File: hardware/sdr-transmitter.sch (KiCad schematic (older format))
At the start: 0 parts

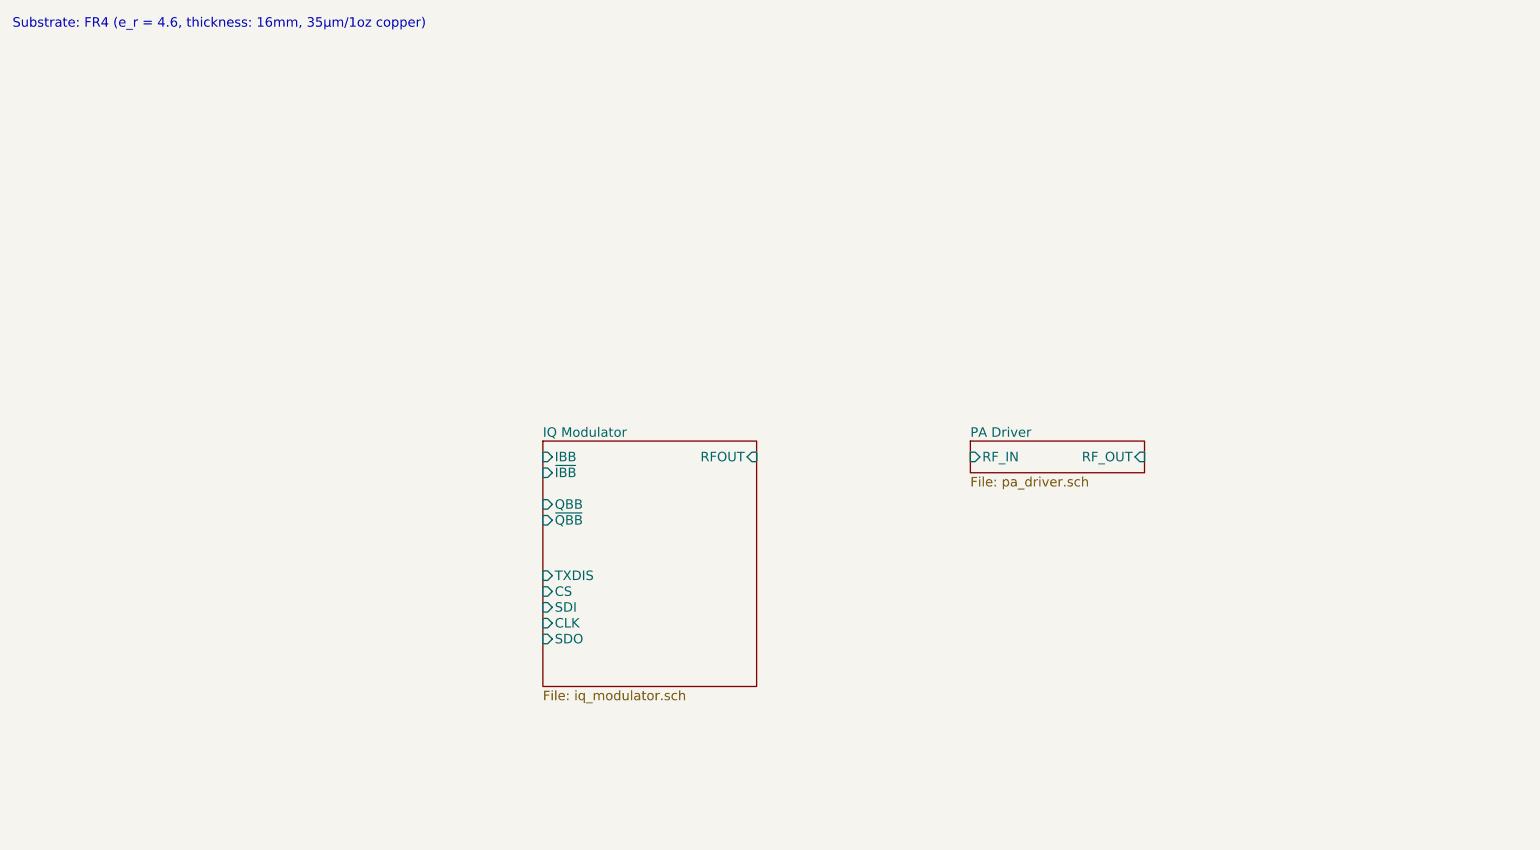
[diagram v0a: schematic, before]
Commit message: Add PA schematic
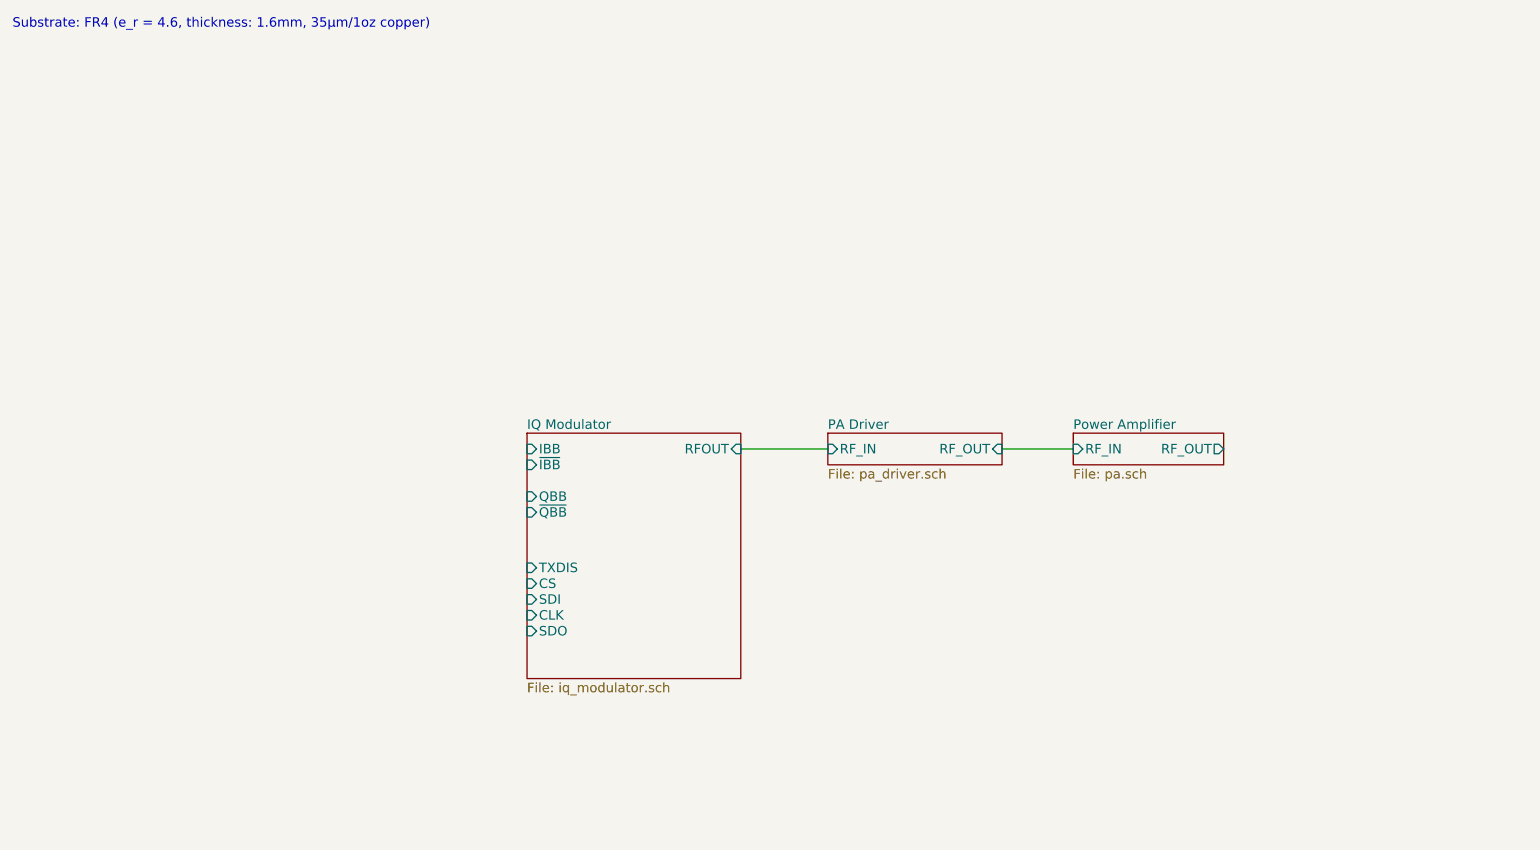
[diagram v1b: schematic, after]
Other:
- note added: "Substrate: FR4 (e_r = 4.6, thickness: 1.6mm, 35µm/1oz copper)"
- note removed: "Substrate: FR4 (e_r = 4.6, thickness: 16mm, 35µm/1oz copper)"
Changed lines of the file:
@@
 LIBS:valves
 LIBS:sdr-transmitter
-LIBS:sdr-transmitter-old
 LIBS:sdr-transmitter-cache
 EELAYER 25 0
@@
 $Descr A4 11693 8268
 encoding utf-8
-Sheet 1 3
+Sheet 1 4
 Title ""
 Date ""
@@
 $EndDescr
 $Sheet
-S 6650 3250 1100 200
+S 5750 3200 1100 200
 U 5A1F13A2
 F0 "PA Driver" 60
 F1 "pa_driver.sch" 60
-F2 "RF_IN" I L 6650 3350 60
-F3 "RF_OUT" I R 7750 3350 60
+F2 "RF_IN" I L 5750 3300 60
+F3 "RF_OUT" I R 6850 3300 60
 $EndSheet
 Text Notes 600  650  0    60   ~ 0
-Substrate: FR4 (e_r = 4.6, thickness: 16mm, 35µm/1oz copper)
+Substrate: FR4 (e_r = 4.6, thickness: 1.6mm, 35µm/1oz copper)
 $Sheet
-S 3950 3250 1350 1550
+S 3850 3200 1350 1550
 U 5A22ED7D
 F0 "IQ Modulator" 60
 F1 "iq_modulator.sch" 60
-F2 "RFOUT" I R 5300 3350 60
-F3 "IBB" I L 3950 3350 60
-F4 "~IBB" I L 3950 3450 60
-F5 "QBB" I L 3950 3650 60
-F6 "TXDIS" I L 3950 4100 60
-F7 "CS" I L 3950 4200 60
-F8 "SDI" I L 3950 4300 60
-F9 "CLK" I L 3950 4400 60
-F10 "SDO" I L 3950 4500 60
-F11 "~QBB" I L 3950 3750 60
+F2 "RFOUT" I R 5200 3300 60
+F3 "IBB" I L 3850 3300 60
+F4 "~IBB" I L 3850 3400 60
+F5 "QBB" I L 3850 3600 60
+F6 "TXDIS" I L 3850 4050 60
+F7 "CS" I L 3850 4150 60
+F8 "SDI" I L 3850 4250 60
+F9 "CLK" I L 3850 4350 60
+F10 "SDO" I L 3850 4450 60
+F11 "~QBB" I L 3850 3700 60
 $EndSheet
+$Sheet
+S 7300 3200 950  200
+U 5A2AAB8B
+F0 "Power Amplifier" 60
+F1 "pa.sch" 60
+F2 "RF_IN" I L 7300 3300 60
+F3 "RF_OUT" O R 8250 3300 60
+$EndSheet
+Wire Wire Line
+	5200 3300 5750 3300
+Wire Wire Line
+	6850 3300 7300 3300
 $EndSCHEMATC

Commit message: Update PA matching circuits
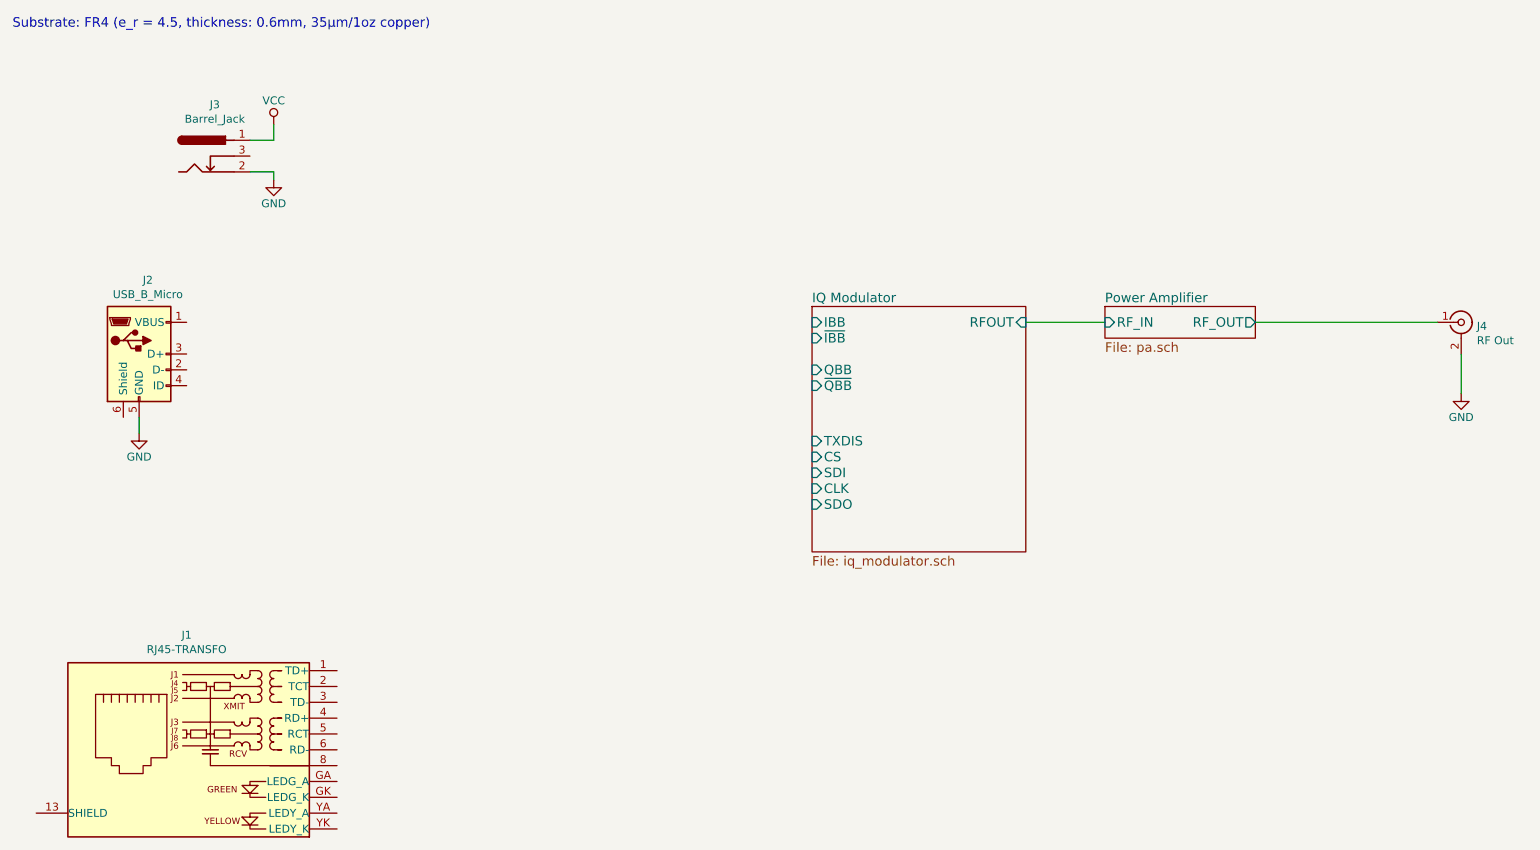
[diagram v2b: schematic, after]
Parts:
- added J1: RJ45-TRANSFO, symbol Connector:RJ45-TRANSFO
- added J2: USB_B_Micro, symbol Connector:USB_B_Micro
- added J3: Barrel_Jack, Connectors:Barrel_Jack_CUI_PJ-036AH-SMT, symbol Connector:Barrel_Jack
- added J4: RF Out, symbol Connector:Conn_Coaxial
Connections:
- net Power Amplifier/RF_OUT: now also J4.1 (In)
- new net GND: J2.5 (GND), J3.2, J4.2 (Ext)
- new net VCC: J3.1
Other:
- note added: "Substrate: FR4 (e_r = 4.5, thickness: 0.6mm, 35µm/1oz copper)"
- note removed: "Substrate: FR4 (e_r = 4.6, thickness: 1.6mm, 35µm/1oz copper)"
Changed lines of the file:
@@
-EESchema Schematic File Version 2
-LIBS:power
-LIBS:device
-LIBS:switches
-LIBS:relays
-LIBS:motors
-LIBS:transistors
-LIBS:conn
-LIBS:linear
-LIBS:regul
-LIBS:74xx
-LIBS:cmos4000
-LIBS:adc-dac
-LIBS:memory
-LIBS:xilinx
-LIBS:microcontrollers
-LIBS:dsp
-LIBS:microchip
-LIBS:analog_switches
-LIBS:motorola
-LIBS:texas
-LIBS:intel
-LIBS:audio
-LIBS:interface
-LIBS:digital-audio
-LIBS:philips
-LIBS:display
-LIBS:cypress
-LIBS:siliconi
-LIBS:opto
-LIBS:atmel
-LIBS:contrib
-LIBS:valves
-LIBS:sdr-transmitter
+EESchema Schematic File Version 4
 LIBS:sdr-transmitter-cache
-EELAYER 25 0
+EELAYER 26 0
 EELAYER END
 $Descr A4 11693 8268
 encoding utf-8
-Sheet 1 4
+Sheet 1 3
 Title ""
 Date ""
@@
 Comment4 ""
 $EndDescr
+Text Notes 600  650  0    60   ~ 0
+Substrate: FR4 (e_r = 4.5, thickness: 0.6mm, 35µm/1oz copper)
 $Sheet
-S 5750 3200 1100 200
-U 5A1F13A2
-F0 "PA Driver" 60
-F1 "pa_driver.sch" 60
-F2 "RF_IN" I L 5750 3300 60
-F3 "RF_OUT" I R 6850 3300 60
-$EndSheet
-Text Notes 600  650  0    60   ~ 0
-Substrate: FR4 (e_r = 4.6, thickness: 1.6mm, 35µm/1oz copper)
-$Sheet
-S 3850 3200 1350 1550
+S 5650 2400 1350 1550
 U 5A22ED7D
 F0 "IQ Modulator" 60
 F1 "iq_modulator.sch" 60
-F2 "RFOUT" I R 5200 3300 60
-F3 "IBB" I L 3850 3300 60
-F4 "~IBB" I L 3850 3400 60
-F5 "QBB" I L 3850 3600 60
-F6 "TXDIS" I L 3850 4050 60
-F7 "CS" I L 3850 4150 60
-F8 "SDI" I L 3850 4250 60
-F9 "CLK" I L 3850 4350 60
-F10 "SDO" I L 3850 4450 60
-F11 "~QBB" I L 3850 3700 60
+F2 "RFOUT" I R 7000 2500 60
+F3 "IBB" I L 5650 2500 60
+F4 "~IBB" I L 5650 2600 60
+F5 "QBB" I L 5650 2800 60
+F6 "TXDIS" I L 5650 3250 60
+F7 "CS" I L 5650 3350 60
+F8 "SDI" I L 5650 3450 60
+F9 "CLK" I L 5650 3550 60
+F10 "SDO" I L 5650 3650 60
+F11 "~QBB" I L 5650 2900 60
 $EndSheet
 $Sheet
-S 7300 3200 950  200
+S 7500 2400 950  200
 U 5A2AAB8B
 F0 "Power Amplifier" 60
 F1 "pa.sch" 60
-F2 "RF_IN" I L 7300 3300 60
-F3 "RF_OUT" O R 8250 3300 60
+F2 "RF_IN" I L 7500 2500 60
+F3 "RF_OUT" O R 8450 2500 60
 $EndSheet
+$Comp
+L power:GND #PWR04
+U 1 1 5A2AACDD
+P 9750 2950
+F 0 "#PWR04" H 9750 2700 50  0001 C CNN
+F 1 "GND" H 9750 2800 50  0000 C CNN
+F 2 "" H 9750 2950 50  0001 C CNN
+F 3 "" H 9750 2950 50  0001 C CNN
+	1    9750 2950
+	1    0    0    -1
+$EndComp
 Wire Wire Line
-	5200 3300 5750 3300
+	9750 2700 9750 2950
 Wire Wire Line
-	6850 3300 7300 3300
+	8450 2500 9600 2500
+$Comp
+L power:GND #PWR03
+U 1 1 5A2AC08A
+P 2250 1600
+F 0 "#PWR03" H 2250 1350 50  0001 C CNN
+F 1 "GND" H 2250 1450 50  0000 C CNN
+F 2 "" H 2250 1600 50  0001 C CNN
+F 3 "" H 2250 1600 50  0001 C CNN
+	1    2250 1600
+	1    0    0    -1
+$EndComp
+Wire Wire Line
+	2100 1550 2250 1550
+Wire Wire Line
+	2250 1550 2250 1600
+$Comp
+L power:VCC #PWR02
+U 1 1 5A2AC12B
+P 2250 1250
+F 0 "#PWR02" H 2250 1100 50  0001 C CNN
+F 1 "VCC" H 2250 1400 50  0000 C CNN
+F 2 "" H 2250 1250 50  0001 C CNN
+F 3 "" H 2250 1250 50  0001 C CNN
+	1    2250 1250
+	1    0    0    -1
+$EndComp
+Wire Wire Line
+	2100 1350 2250 1350
+Wire Wire Line
+	2250 1350 2250 1250
+$Comp
+L power:GND #PWR01
+U 1 1 5A2AC762
+P 1400 3200
+F 0 "#PWR01" H 1400 2950 50  0001 C CNN
+F 1 "GND" H 1400 3050 50  0000 C CNN
+F 2 "" H 1400 3200 50  0001 C CNN
+F 3 "" H 1400 3200 50  0001 C CNN
+	1    1400 3200
+	1    0    0    -1
+$EndComp
+Wire Wire Line
+	1400 3100 1400 3200
+$Comp
+L Connector:RJ45-TRANSFO J1
+U 1 1 5A3231AA
+P 1350 5200
+F 0 "J1" H 1000 5925 50  0000 C CNN
+F 1 "RJ45-TRANSFO" H 1000 5834 50  0000 C CNN
+F 2 "" H 1350 5700 50  0001 C CNN
+F 3 "~" H 1450 5800 50  0001 C CNN
+	1    1350 5200
+	-1   0    0    -1
+$EndComp
+$Comp
+L Connector:USB_B_Micro J2
+U 1 1 5A323CBA
+P 1400 2700
+F 0 "J2" H 1455 3167 50  0000 C CNN
+F 1 "USB_B_Micro" H 1455 3076 50  0000 C CNN
+F 2 "" H 1550 2650 50  0001 C CNN
+F 3 "~" H 1550 2650 50  0001 C CNN
+	1    1400 2700
+	1    0    0    -1
+$EndComp
+$Comp
+L Connector:Barrel_Jack J3
+U 1 1 5A3242D7
+P 1800 1450
+F 0 "J3" H 1878 1775 50  0000 C CNN
+F 1 "Barrel_Jack" H 1878 1684 50  0000 C CNN
+F 2 "Connectors:Barrel_Jack_CUI_PJ-036AH-SMT" H 1850 1410 50  0001 C CNN
+F 3 "~" H 1850 1410 50  0001 C CNN
+	1    1800 1450
+	1    0    0    -1
+$EndComp
+$Comp
+L Connector:Conn_Coaxial J4
+U 1 1 5A324912
+P 9750 2500
+F 0 "J4" H 9849 2476 50  0000 L CNN
+F 1 "RF Out" H 9849 2385 50  0000 L CNN
+F 2 "" H 9750 2500 50  0001 C CNN
+F 3 "" H 9750 2500 50  0001 C CNN
+	1    9750 2500
+	1    0    0    -1
+$EndComp
+Wire Wire Line
+	7000 2500 7500 2500
 $EndSCHEMATC
